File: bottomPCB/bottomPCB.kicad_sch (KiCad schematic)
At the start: 46 parts, among them J1 Conn_01x03_Pin, J2 Conn_02x03_Odd_Even, J3 Conn_01x02, J4 Conn_02x03_Odd_Even, J5 1-84953-1, J6 1-84953-1, J7 1-84953-1, J8 1-84953-1, U1 ESP32-WROOM-32, U2 XT30_horizontal, U8 LM1117IMPX-3_3_NOPB, U9 LM1117IMPX-3_3_NOPB

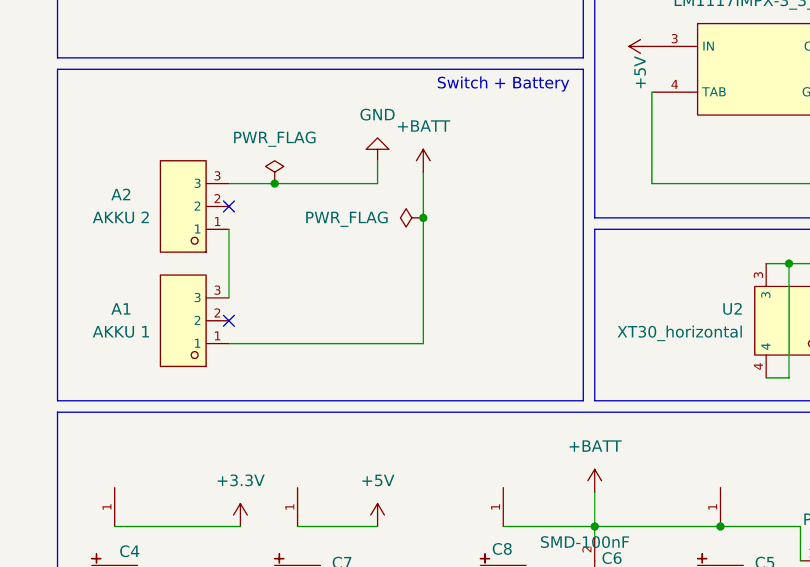
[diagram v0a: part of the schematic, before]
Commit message: added xt30 horizontal as switch
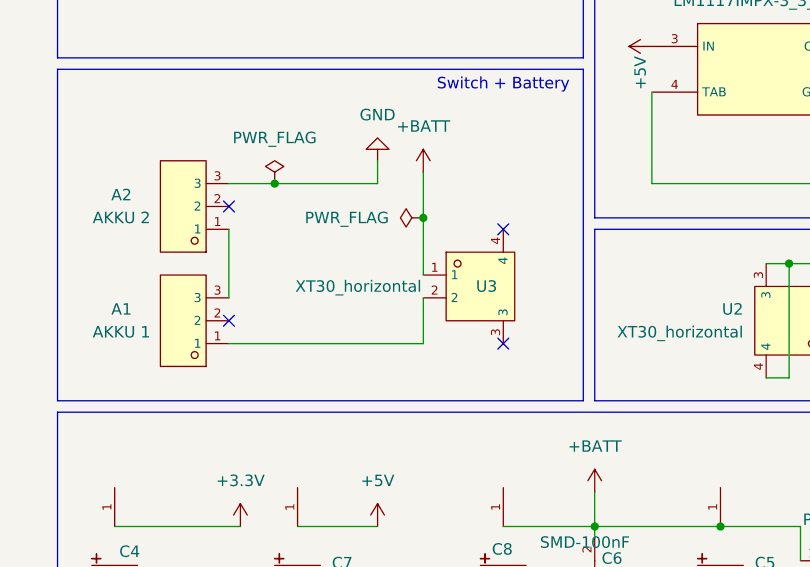
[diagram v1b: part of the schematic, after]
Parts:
- added U3: XT30_horizontal, BohleBots:CONN-TH_XT30PW-M, symbol bohlebots.lib:XT30_horizontal
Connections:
- net +BATT: now also U3.1; no longer A1.1
- new net: A1.1, U3.2
- no-connect marks 18 -> 20
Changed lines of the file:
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@@
 	)
 	(junction
-		(at 195.58 67.31)
-		(diameter 0)
-		(color 0 0 0 0)
-	)
-	(junction
 		(at 248.92 48.26)
 		(diameter 0)
@@
 	)
 	(junction
+		(at 195.58 67.31)
+		(diameter 0)
+		(color 0 0 0 0)
+	)
+	(junction
 		(at 181.61 149.86)
 		(diameter 0)
@@
 	)
 	(no_connect
+		(at 204.47 81.28)
+	)
+	(no_connect
 		(at 168.91 30.48)
 	)
 	(no_connect
+		(at 204.47 68.58)
+	)
+	(no_connect
 		(at 173.99 66.04)
 	)
@@
 	(wire
 		(pts
-			(xy 195.58 67.31) (xy 195.58 81.28)
-		)
-		(stroke
-			(width 0)
-			(type default)
-		)
-	)
-	(wire
-		(pts
 			(xy 49.53 111.76) (xy 49.53 110.49)
 		)
@@
 	(wire
 		(pts
+			(xy 195.58 76.2) (xy 195.58 81.28)
+		)
+		(stroke
+			(width 0)
+			(type default)
+		)
+	)
+	(wire
+		(pts
 			(xy 267.97 132.08) (xy 267.97 134.62)
 		)
@@
 	(wire
 		(pts
+			(xy 195.58 67.31) (xy 195.58 73.66)
+		)
+		(stroke
+			(width 0)
+			(type default)
+		)
+	)
+	(wire
+		(pts
 			(xy 270.51 132.08) (xy 267.97 132.08)
 		)
@@
 					(unit 1)
 				)
+			)
+		)
+	)
+	(symbol
+		(lib_id "bohlebots.lib:XT30_horizontal")
+		(at 200.66 74.93 0)
+		(unit 1)
+		(exclude_from_sim no)
+		(in_bom yes)
+		(on_board yes)
+		(dnp no)
+		(property "Reference" "U3"
+			(at 201.422 74.93 0)
+			(effects
+				(font
+					(size 1.27 1.27)
+				)
+				(justify left)
+			)
+		)
+		(property "Value" "XT30_horizontal"
+			(at 181.356 74.93 0)
+			(effects
+				(font
+					(size 1.27 1.27)
+				)
+				(justify left)
+			)
+		)
+		(property "Footprint" "BohleBots:CONN-TH_XT30PW-M"
+			(at 200.66 85.09 0)
+			(effects
+				(font
+					(size 1.27 1.27)
+					(italic yes)
+				)
+				(hide yes)
+			)
+		)
+		(property "Datasheet" "https://cn.bing.com/search?q=datasheet: XT30PW-M"
+			(at 198.374 74.803 0)
+			(effects
+				(font
+					(size 1.27 1.27)
+				)
+				(justify left)
+				(hide yes)
+			)
+		)
+		(property "Description" ""
+			(at 200.66 74.93 0)
+			(effects
+				(font
+					(size 1.27 1.27)
+				)
+				(hide yes)
+			)
+		)
+		(property "LCSC" "C431092"
+			(at 200.66 74.93 0)
+			(effects
+				(font
+					(size 1.27 1.27)
+				)
+				(hide yes)
+			)
+		)
+		(pin "1"
+		)
+		(pin "2"
+		)
+		(pin "3"
+		)
+		(pin "4"
+		)
+		(instances
+			(project "bottomPCB"
+				(path "/530b96b6-d439-440e-a48e-82f0fe8f4bb1"
+					(reference "U3")
+					(unit 1)
+				)

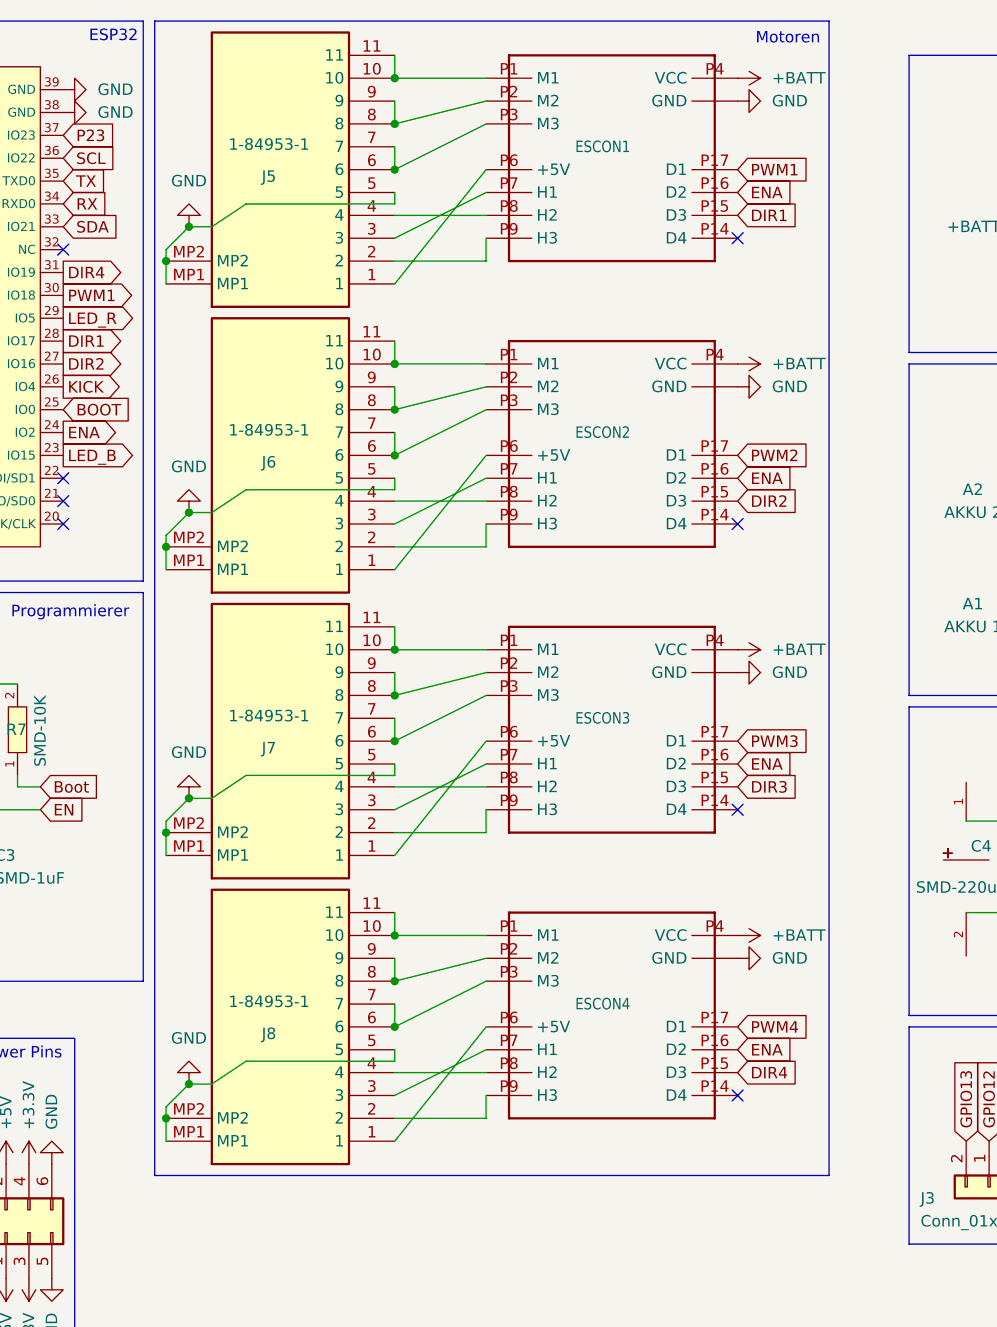
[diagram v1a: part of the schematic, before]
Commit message: replaced smd connectors for ec flat with BohleBots standard
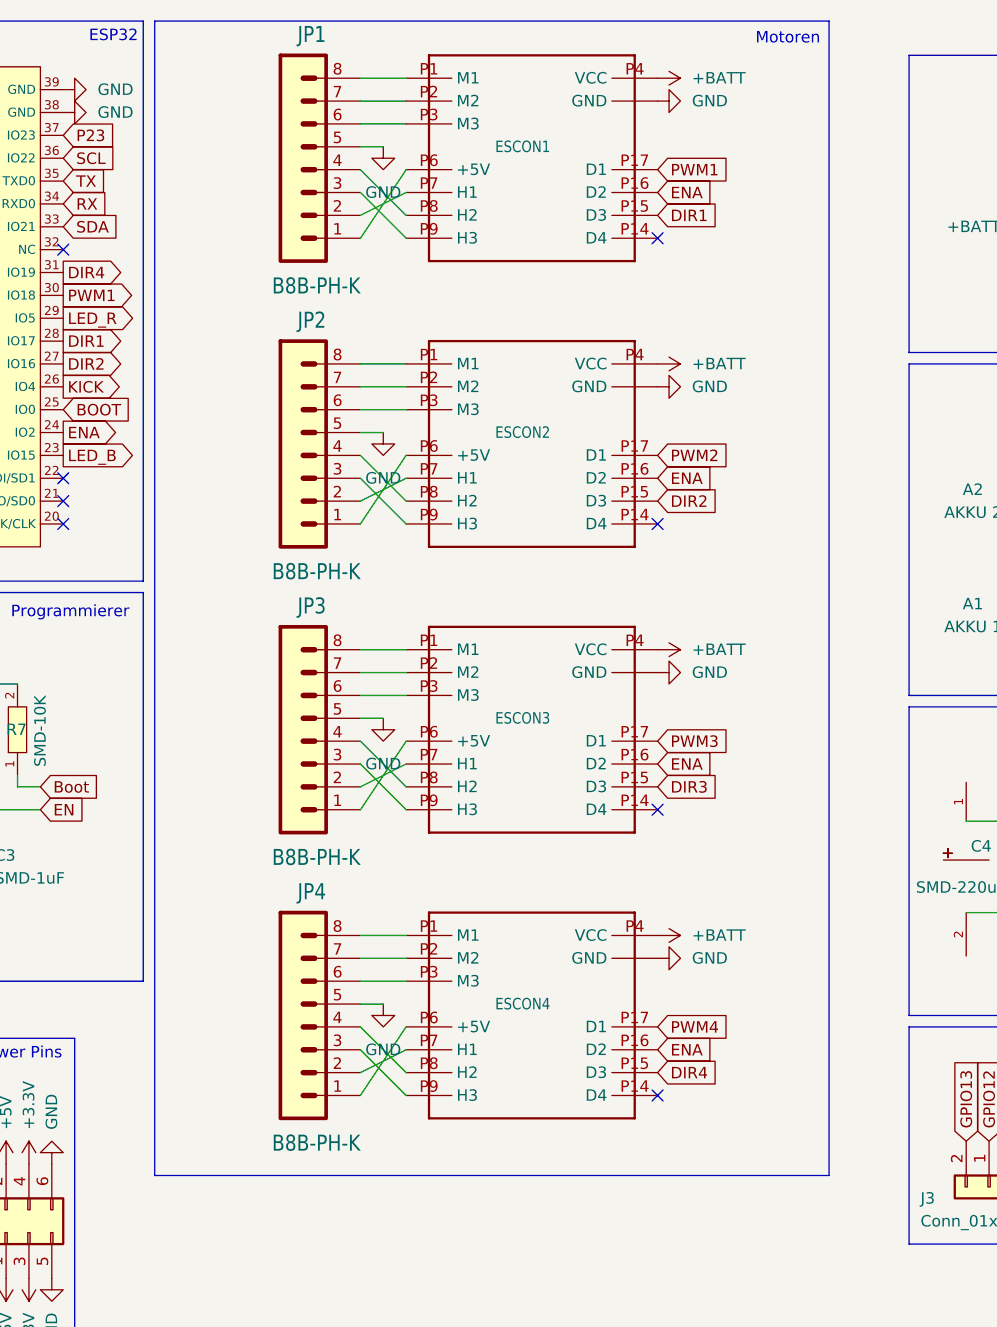
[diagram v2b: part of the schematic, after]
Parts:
- removed J5, J6, J7, J8: 1-84953-1, 1-84953-1:1849531, symbol 1-84953-1:1-84953-1
- added JP1, JP2, JP3, JP4: B8B-PH-K, Connector_JST:JST_PH_B8B-PH-K_1x08_P2.00mm_Vertical, symbol main_backupboard-eagle-import:B8B-PH-K
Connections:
- net GND: now also JP1.5, JP2.5, JP3.5, JP4.5
- net at ESCON3.P1 (M1): now also JP3.8
- net at ESCON3.P2 (M2): now also JP3.7
- net at ESCON3.P3 (M3): now also JP3.6
- net at ESCON3.P6 (+5V): now also JP3.1
- net at ESCON3.P7 (H1): now also JP3.2
- net at ESCON3.P8 (H2): now also JP3.4
- net at ESCON3.P9 (H3): now also JP3.3
- net at ESCON1.P6 (+5V): now also JP1.1
- net at ESCON1.P1 (M1): now also JP1.8
- net at ESCON1.P9 (H3): now also JP1.3
- net at ESCON1.P7 (H1): now also JP1.2
- net at ESCON1.P8 (H2): now also JP1.4
- net at ESCON1.P3 (M3): now also JP1.6
- net at ESCON1.P2 (M2): now also JP1.7
- net at ESCON4.P6 (+5V): now also JP4.1
- net at ESCON4.P1 (M1): now also JP4.8
- net at ESCON4.P9 (H3): now also JP4.3
- net at ESCON4.P7 (H1): now also JP4.2
- net at ESCON4.P8 (H2): now also JP4.4
- net at ESCON4.P3 (M3): now also JP4.6
- net at ESCON4.P2 (M2): now also JP4.7
- net at ESCON2.P6 (+5V): now also JP2.1
- net at ESCON2.P1 (M1): now also JP2.8
- net at ESCON2.P9 (H3): now also JP2.3
- net at ESCON2.P7 (H1): now also JP2.2
- net at ESCON2.P8 (H2): now also JP2.4
- net at ESCON2.P3 (M3): now also JP2.6
- net at ESCON2.P2 (M2): now also JP2.7
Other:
- moved on the sheet: ESCON1, ESCON2, ESCON3, ESCON4

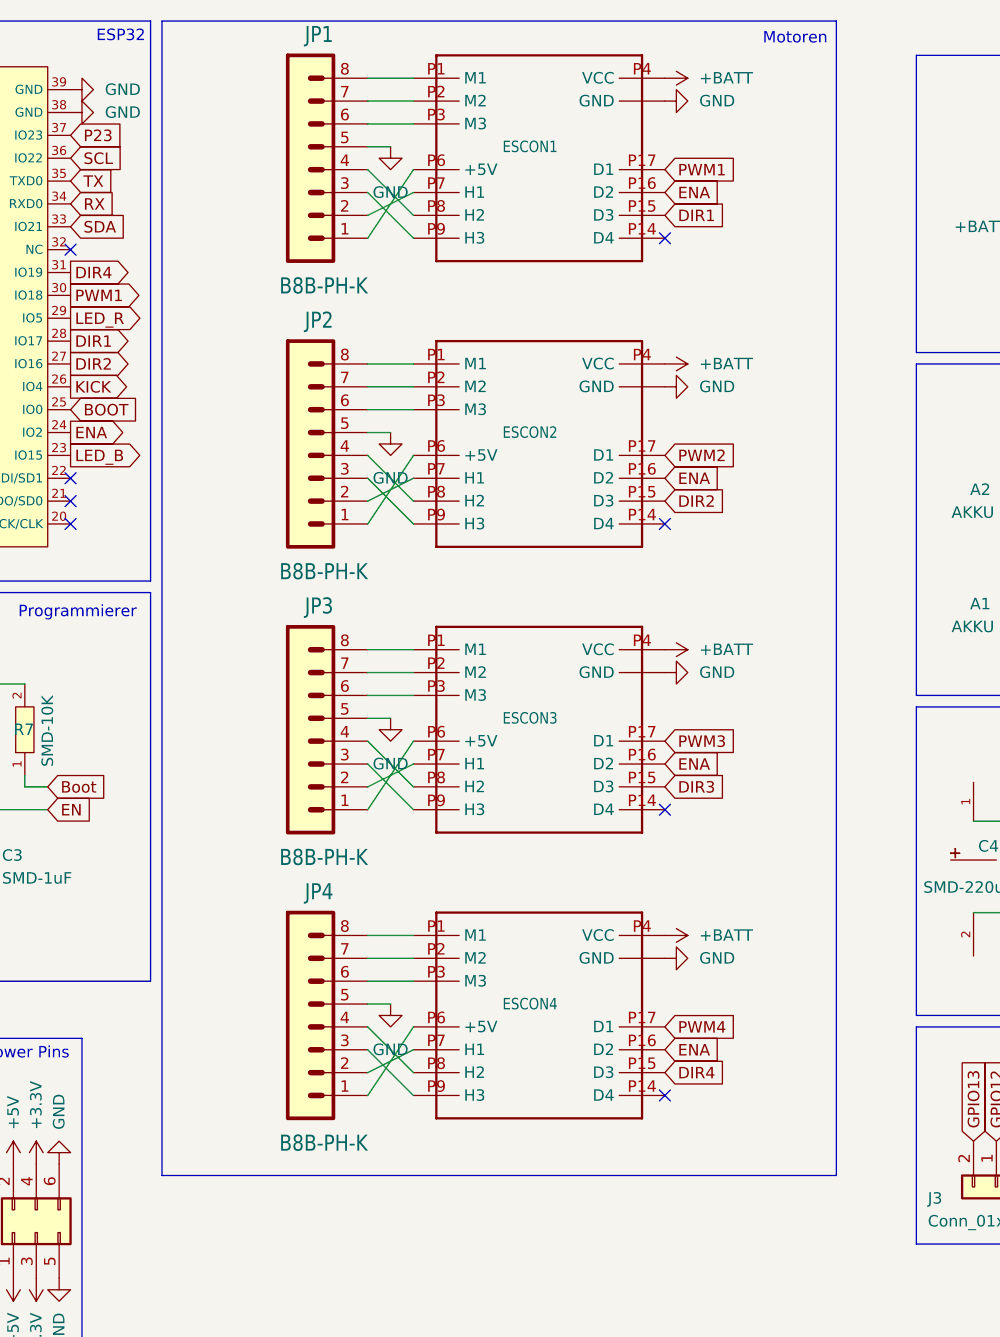
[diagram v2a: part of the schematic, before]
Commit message: replaced escon drivers with vertical breakout board
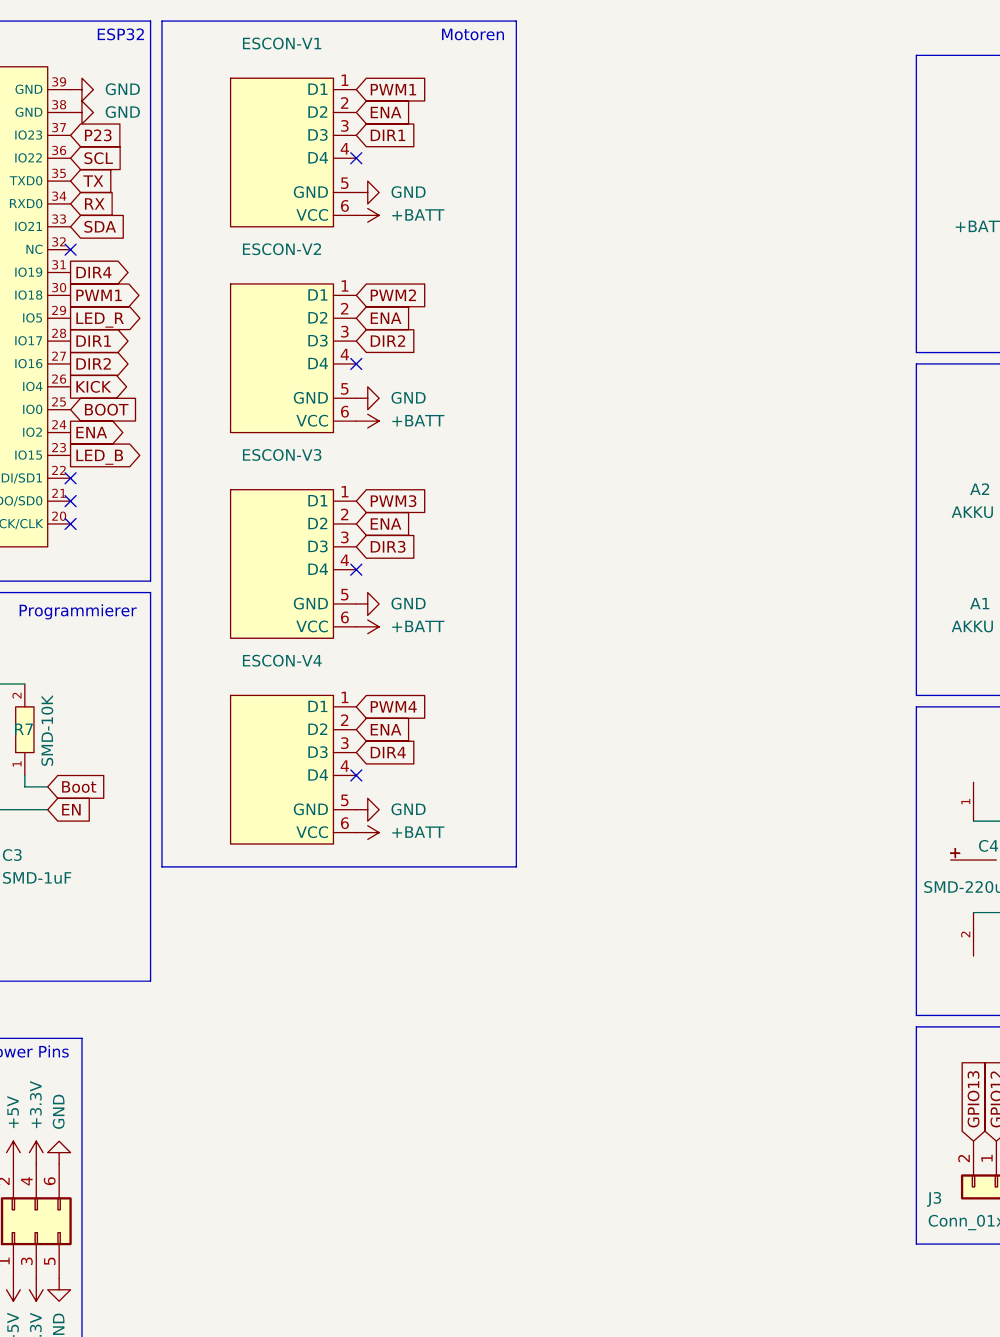
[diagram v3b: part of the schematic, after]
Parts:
- removed ESCON1, ESCON2, ESCON3, ESCON4: 24_2, BohleBots:ESCOM_24_2, symbol bohlebots.lib:ESCOM_24/2
- removed JP1, JP2, JP3, JP4: B8B-PH-K, Connector_JST:JST_PH_B8B-PH-K_1x08_P2.00mm_Vertical, symbol main_backupboard-eagle-import:B8B-PH-K
- added ESCON-V1, ESCON-V2, ESCON-V3, ESCON-V4: ~, sarcat:ESCON-V, symbol sarcat:ESCON-V
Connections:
- net +BATT: now also ESCON-V1.6 (VCC), ESCON-V2.6 (VCC), ESCON-V3.6 (VCC), ESCON-V4.6 (VCC)
- net DIR1: now also ESCON-V1.3 (D3)
- net DIR2: now also ESCON-V2.3 (D3)
- net DIR3: now also ESCON-V3.3 (D3)
- net DIR4: now also ESCON-V4.3 (D3)
- net ENA: now also ESCON-V1.2 (D2), ESCON-V2.2 (D2), ESCON-V3.2 (D2), ESCON-V4.2 (D2)
- net GND: now also ESCON-V1.5 (GND), ESCON-V2.5 (GND), ESCON-V3.5 (GND), ESCON-V4.5 (GND)
- net PWM1: now also ESCON-V1.1 (D1)
- net PWM2: now also ESCON-V2.1 (D1)
- net PWM3: now also ESCON-V3.1 (D1)
- net PWM4: now also ESCON-V4.1 (D1)
